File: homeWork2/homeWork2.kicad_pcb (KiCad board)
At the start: 2 copper layers, 113.1 x 52.7 mm, 60 parts, among them J1 Barrel_Jack_Switch_SMT, J2 Conn_01x15_Socket, J3 Conn_01x15_Socket, J4_LCD1 Conn_01x04_Socket_LCD, J5_DFPLAYER1 Conn_01x04_Socket_DFPLAYER, U1 LM7805_TO220

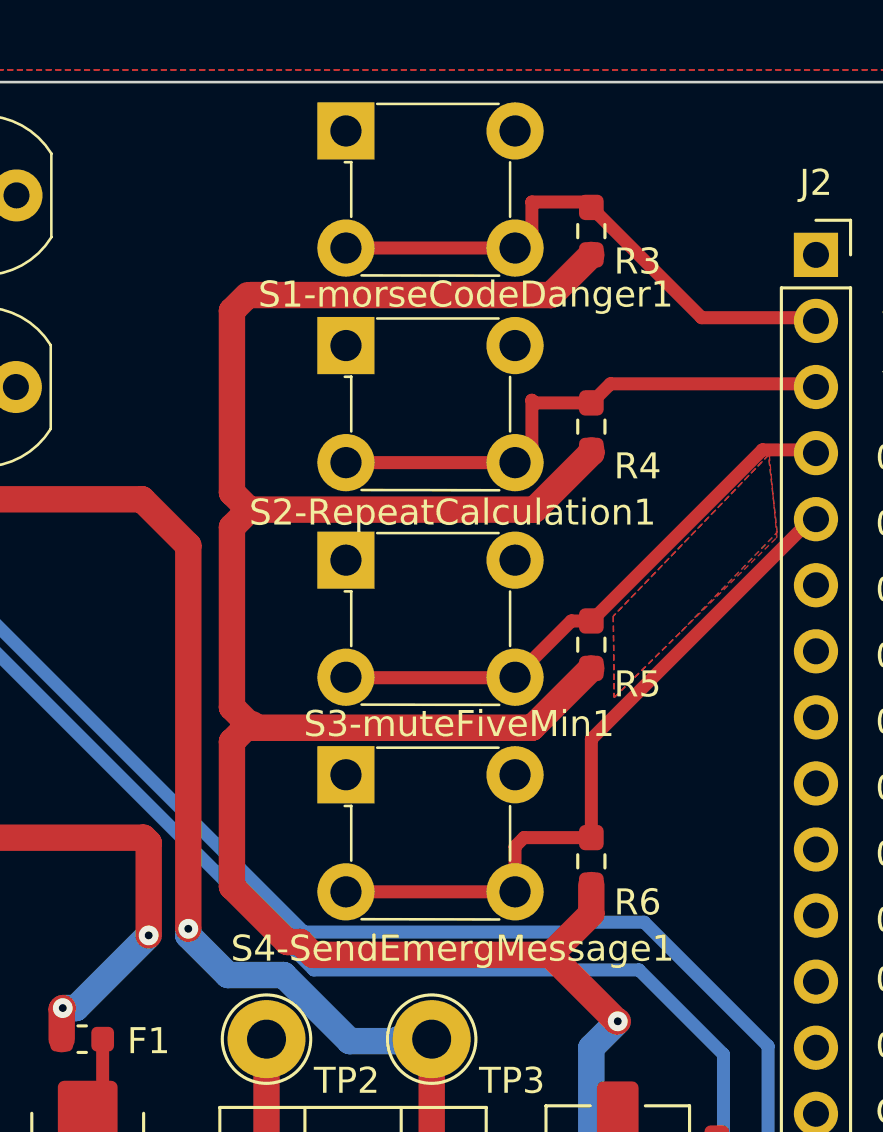
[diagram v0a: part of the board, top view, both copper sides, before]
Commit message: Updated the switches and added 3d model for the switches.
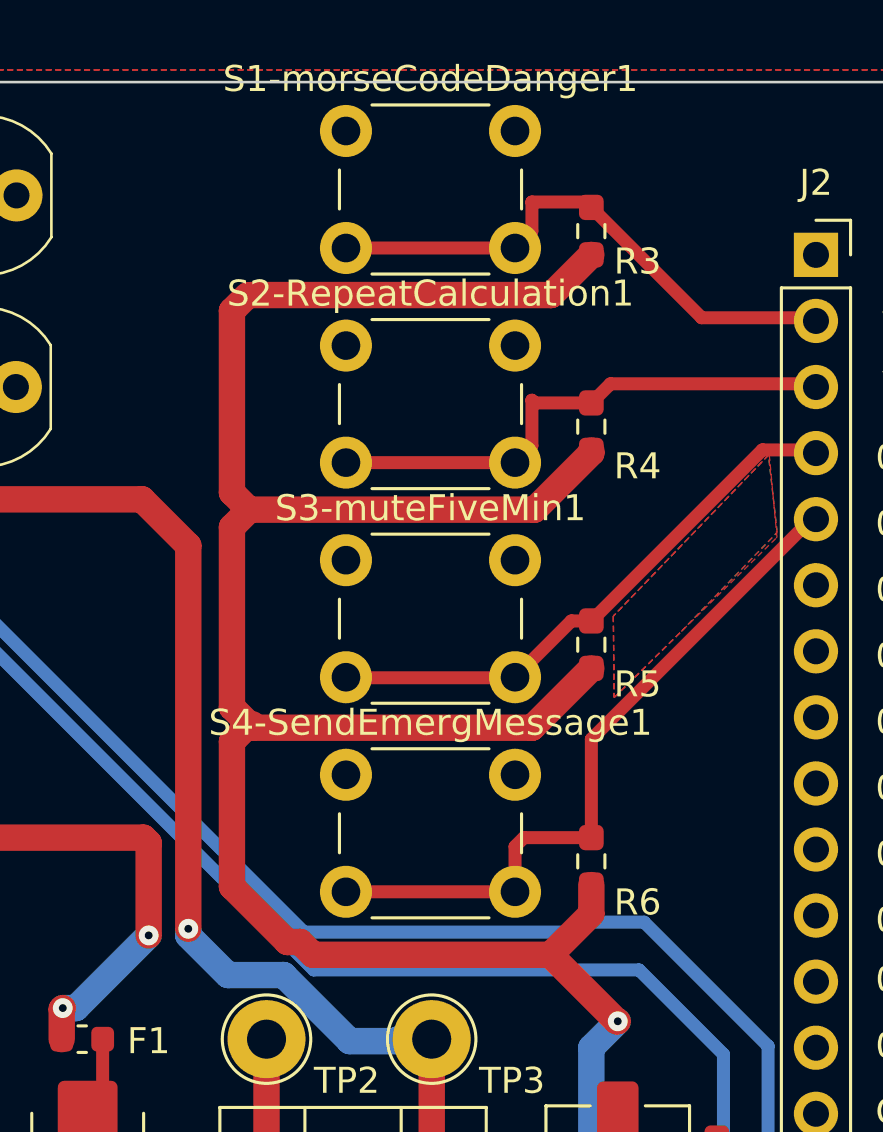
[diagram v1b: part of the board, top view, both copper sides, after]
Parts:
- J4_LCD1: value Conn_01x04_Socket_LCD -> Conn_01x04
- J5_DFPLAYER1: value Conn_01x04_Socket_DFPLAYER -> Conn_01x04
- R1, R7: value 1R -> 1
- R10, R11, R12, R13, R14, R8, R9: value 60 ohm -> 62
- R2: value 330R -> 150
- R3, R4, R5, R6: value 10 k -> 10k
- S1-morseCodeDanger1, S2-RepeatCalculation1, S3-muteFiveMin1, S4-SendEmergMessage1: footprint GeneralPurposeAlarmDevicePCB:Switch_Tactile_THT_6x6mm -> Button_Switch_THT:SW_PUSH_6mm_H9.5mm
